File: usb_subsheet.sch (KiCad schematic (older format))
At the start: 10 parts

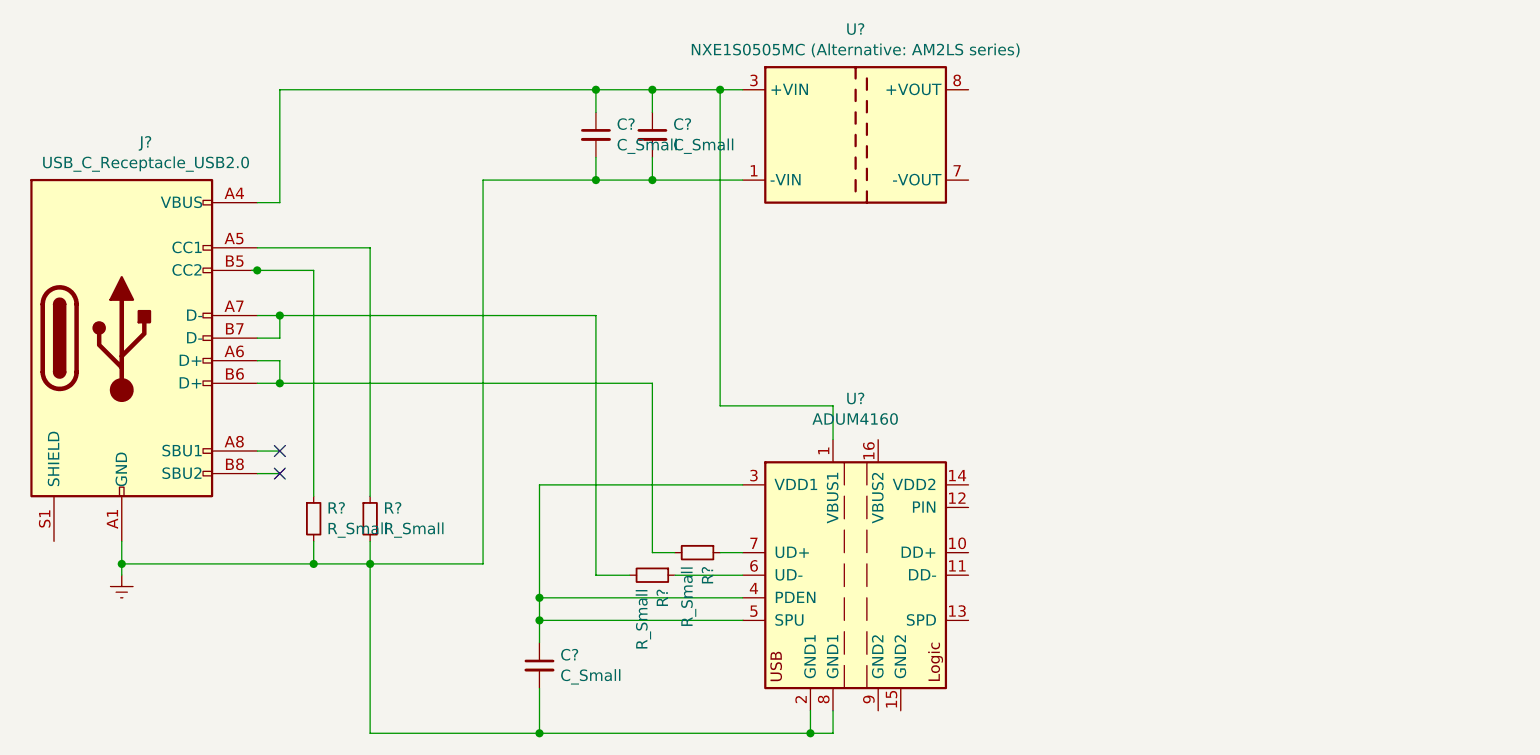
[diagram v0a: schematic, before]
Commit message: [usb]: wire isolator with dcdc + hierarchy
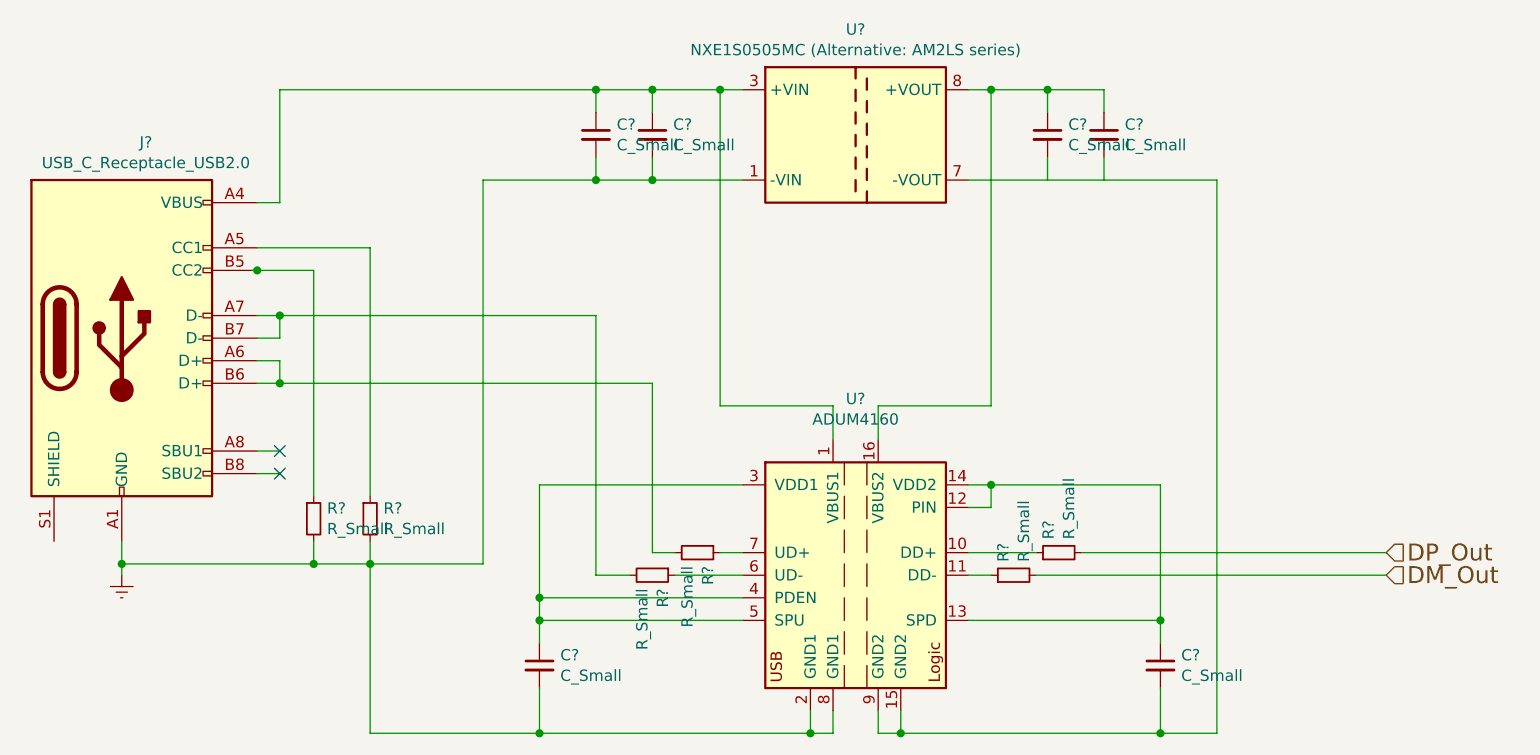
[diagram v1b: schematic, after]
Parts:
- added C? (x3): C_Small, symbol Device:C_Small
- added R? (x2): R_Small, symbol Device:R_Small
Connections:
- net labels added: DM_Out, DP_Out
- wire segments 58 -> 87
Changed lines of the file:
@@
 Wire Wire Line
 	5300 2350 5400 2350
+$Comp
+L Device:R_Small R?
+U 1 1 6215EE9A
+P 6600 4500
+F 0 "R?" H 6659 4546 50  0000 L CNN
+F 1 "R_Small" H 6659 4455 50  0000 L CNN
+F 2 "" H 6600 4500 50  0001 C CNN
+F 3 "~" H 6600 4500 50  0001 C CNN
+	1    6600 4500
+	0    -1   -1   0
+$EndComp
+$Comp
+L Device:R_Small R?
+U 1 1 6215EEA0
+P 6800 4400
+F 0 "R?" H 6859 4446 50  0000 L CNN
+F 1 "R_Small" H 6859 4355 50  0000 L CNN
+F 2 "" H 6800 4400 50  0001 C CNN
+F 3 "~" H 6800 4400 50  0001 C CNN
+	1    6800 4400
+	0    -1   -1   0
+$EndComp
+Wire Wire Line
+	6000 5100 6000 5200
+Wire Wire Line
+	6000 5200 6100 5200
+Wire Wire Line
+	6100 5200 6100 5100
+Wire Wire Line
+	6000 3900 6000 3750
+Wire Wire Line
+	6000 3750 6500 3750
+$Comp
+L Device:C_Small C?
+U 1 1 62187507
+P 7250 4900
+F 0 "C?" H 7342 4946 50  0000 L CNN
+F 1 "C_Small" H 7342 4855 50  0000 L CNN
+F 2 "" H 7250 4900 50  0001 C CNN
+F 3 "~" H 7250 4900 50  0001 C CNN
+	1    7250 4900
+	1    0    0    -1
+$EndComp
+Connection ~ 6100 5200
+Wire Wire Line
+	7250 5200 7250 5000
+Wire Wire Line
+	6400 4500 6500 4500
+Wire Wire Line
+	6400 4400 6700 4400
+Wire Wire Line
+	7250 4100 7250 4700
+Wire Wire Line
+	6400 4100 6500 4100
+Wire Wire Line
+	6100 5200 7250 5200
+Wire Wire Line
+	6400 4200 6500 4200
+Wire Wire Line
+	6500 4200 6500 4100
+Connection ~ 6500 4100
+Wire Wire Line
+	6500 4100 7250 4100
+Wire Wire Line
+	6400 4700 7250 4700
+Connection ~ 7250 4700
+Wire Wire Line
+	7250 4700 7250 4800
+Text HLabel 8250 4500 2    75   Input ~ 0
+DM_Out
+Text HLabel 8250 4400 2    75   Input ~ 0
+DP_Out
+Wire Wire Line
+	6400 2750 7500 2750
+Wire Wire Line
+	7500 2750 7500 5200
+Wire Wire Line
+	7500 5200 7250 5200
+Connection ~ 7250 5200
+$Comp
+L Device:C_Small C?
+U 1 1 621B7E73
+P 7000 2550
+F 0 "C?" H 7092 2596 50  0000 L CNN
+F 1 "C_Small" H 7092 2505 50  0000 L CNN
+F 2 "" H 7000 2550 50  0001 C CNN
+F 3 "~" H 7000 2550 50  0001 C CNN
+	1    7000 2550
+	1    0    0    -1
+$EndComp
+Wire Wire Line
+	7000 2450 7000 2350
+Wire Wire Line
+	7000 2650 7000 2750
+$Comp
+L Device:C_Small C?
+U 1 1 621B7E7B
+P 6750 2550
+F 0 "C?" H 6842 2596 50  0000 L CNN
+F 1 "C_Small" H 6842 2505 50  0000 L CNN
+F 2 "" H 6750 2550 50  0001 C CNN
+F 3 "~" H 6750 2550 50  0001 C CNN
+	1    6750 2550
+	1    0    0    -1
+$EndComp
+Wire Wire Line
+	6750 2650 6750 2750
+Wire Wire Line
+	6750 2450 6750 2350
+Wire Wire Line
+	6400 2350 6500 2350
+Wire Wire Line
+	6750 2350 7000 2350
+Connection ~ 6750 2350
+Wire Wire Line
+	6500 2350 6500 3750
+Connection ~ 6500 2350
+Wire Wire Line
+	6500 2350 6750 2350
+Wire Wire Line
+	6900 4400 8250 4400
+Wire Wire Line
+	6700 4500 8250 4500
 $EndSCHEMATC

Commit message: [minor]
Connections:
- net labels removed: Earth
- wire segments 87 -> 86
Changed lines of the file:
@@
 	3750 4450 3500 4450
 Connection ~ 3500 4450
-$Comp
-L power:Earth #PWR?
-U 1 1 620DE109
-P 2650 4500
-F 0 "#PWR?" H 2650 4250 50  0001 C CNN
-F 1 "Earth" H 2650 4350 50  0001 C CNN
-F 2 "" H 2650 4500 50  0001 C CNN
-F 3 "~" H 2650 4500 50  0001 C CNN
-	1    2650 4500
-	1    0    0    -1
-$EndComp
-Wire Wire Line
-	2650 4450 2650 4500
-Connection ~ 2650 4450
 Connection ~ 3350 3350
 Connection ~ 3350 3650
